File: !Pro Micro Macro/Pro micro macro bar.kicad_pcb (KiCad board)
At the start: 2 copper layers, 61.9 x 61.9 mm, 19 parts, among them U1 ProMicro

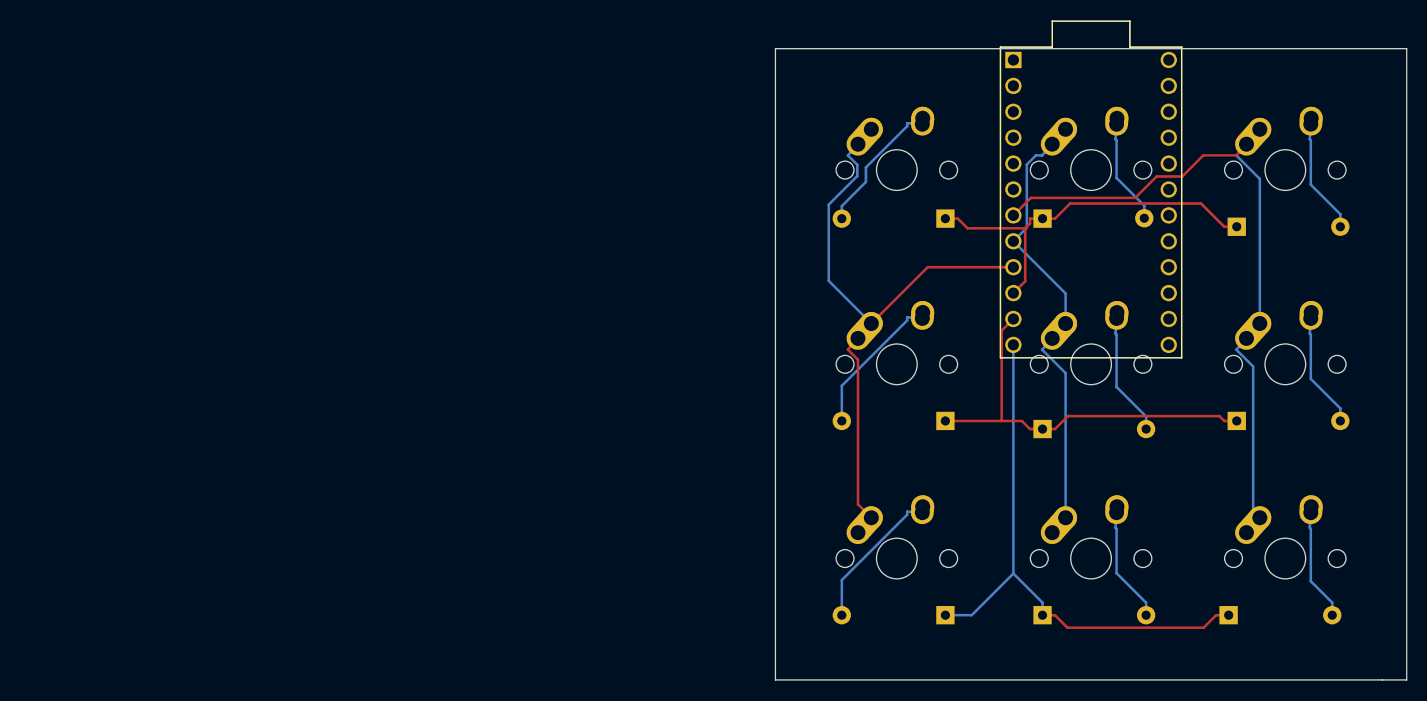
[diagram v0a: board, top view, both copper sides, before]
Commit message: Redesigned pro micro
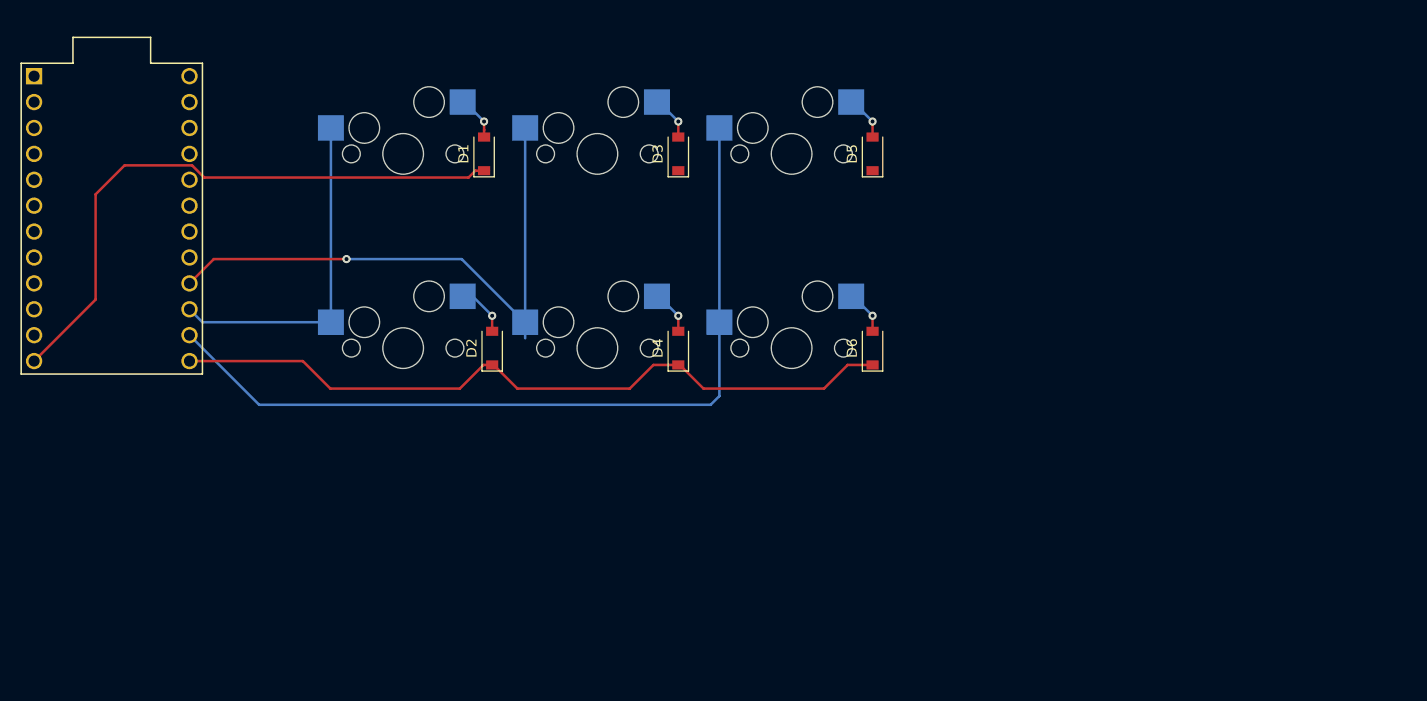
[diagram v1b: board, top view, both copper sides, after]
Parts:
- removed D7, D8, D9: D_Small, Diode_THT:D_A-405_P10.16mm_Horizontal
- removed MX7, MX8, MX9: MX-NoLED, Bases github:MX-1U-NoLED
- D1, D2, D3, D4, D5, D6: footprint Diode_THT:D_A-405_P10.16mm_Horizontal -> random-keyboard-parts:D_SOD-123-Pretty; moved to F.Cu
- MX1, MX2, MX3, MX4, MX5, MX6: footprint Bases github:MX-1U-NoLED -> ! MX bases:MXOnly-1U-Hotswap
- moved U1 96.1 mm to (115.1, 84.1)
- moved D3 52.3 mm to (170.7, 77.8), turned to 90 degrees
- moved MX4 51.5 mm to (162.7, 96.8)
- moved MX3 49.4 mm to (162.7, 77.8)
- moved MX1 48.4 mm to (143.7, 77.8)
- moved MX2 48.4 mm to (143.7, 96.8)
- moved D1 45.7 mm to (151.6, 77.8), turned to 90 degrees
- moved D2 45.0 mm to (152.4, 96.8), turned to 90 degrees
- moved D4 37.9 mm to (170.7, 96.8), turned to 90 degrees
- moved MX5 35.9 mm to (181.8, 77.8)
- moved MX6 35.9 mm to (181.8, 96.8)
- moved D5 31.7 mm to (189.7, 77.8), turned to 90 degrees
- moved D6 31.0 mm to (189.7, 96.8), turned to 90 degrees
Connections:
- D3 pad 1: ROW2 -> ROW0
- D4 pad 1: ROW0 -> ROW1
- D5 pad 1: ROW1 -> ROW0
- D6 pad 1: ROW2 -> ROW1
- MX3 pad 1: COL0 -> COL1
- MX5 pad 1: COL1 -> COL2
- MX6 pad 1: COL1 -> COL2
- U1 pad 10: ROW0 -> Net-(U1-Pad10)
- U1 pad 11: ROW1 -> Net-(U1-Pad11)
- U1 pad 12: ROW2 -> ROW0
- U1 pad 13: Net-(U1-Pad13) -> ROW1
- U1 pad 14: Net-(U1-Pad14) -> COL2
- U1 pad 15: Net-(U1-Pad15) -> COL0
- U1 pad 16: Net-(U1-Pad16) -> COL1
- U1 pad 7: COL2 -> Net-(U1-Pad7)
- U1 pad 8: COL1 -> Net-(U1-Pad8)
- U1 pad 9: COL0 -> Net-(U1-Pad9)
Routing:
- net ROW2: track 55.3 -> 0.00 mm
- net ROW1: track 40.1 -> 73.4 mm
- net COL0: track 62.4 -> 33.4 mm
- net ROW0: track 38.0 -> 59.4 mm
- net Net-(D7-Pad2): track 11.9 -> 0.00 mm
- net Net-(D8-Pad2): track 11.9 -> 0.00 mm
- net COL2: track 69.8 -> 81.4 mm
- net Net-(D9-Pad2): track 11.6 -> 0.00 mm
- net COL1: track 46.5 -> 57.1 mm, vias 0 -> 1
- net Net-(D3-Pad2): track 14.9 -> 4.41 mm, vias 0 -> 1
- net Net-(D1-Pad2): track 14.1 -> 4.41 mm, vias 0 -> 1
- net Net-(D2-Pad2): track 14.9 -> 5.20 mm, vias 0 -> 1
- net Net-(D5-Pad2): track 12.7 -> 4.41 mm, vias 0 -> 1
- net Net-(D6-Pad2): track 11.9 -> 4.41 mm, vias 0 -> 1
- net Net-(D4-Pad2): track 11.0 -> 4.41 mm, vias 0 -> 1
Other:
- board outline removed
